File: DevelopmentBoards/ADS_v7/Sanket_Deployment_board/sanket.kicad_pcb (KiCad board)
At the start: 2 copper layers, 95.9 x 92 mm, 42 parts, among them J2 Conn_02x03_Counter_Clockwise, J3 Conn_02x03_Counter_Clockwise, U1 SN74LVC1G17QDCKRQ1

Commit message: ADS-V7, Corrected board setting according to PCB power, placed resistors after the decoupling capacitors
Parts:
- moved R12 12.2 mm to (129.2, 133.6), turned to -90 degrees
- moved R10 6.95 mm to (129.2, 137.5), turned to 90 degrees
- moved J1 3.26 mm to (132.9, 130.4)
- moved L1 1.28 mm to (130.8, 143.2)
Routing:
- net +3V3: track 97.5 -> 92.6 mm
- net Net-(J1-Pin_1): track 6.71 -> 9.95 mm
- net /BurnWire1IN: track 84.9 -> 81.7 mm
- net Net-(J1-Pin_3): track 7.44 -> 4.90 mm
- net Net-(D1-K): track 30.9 -> 32.1 mm

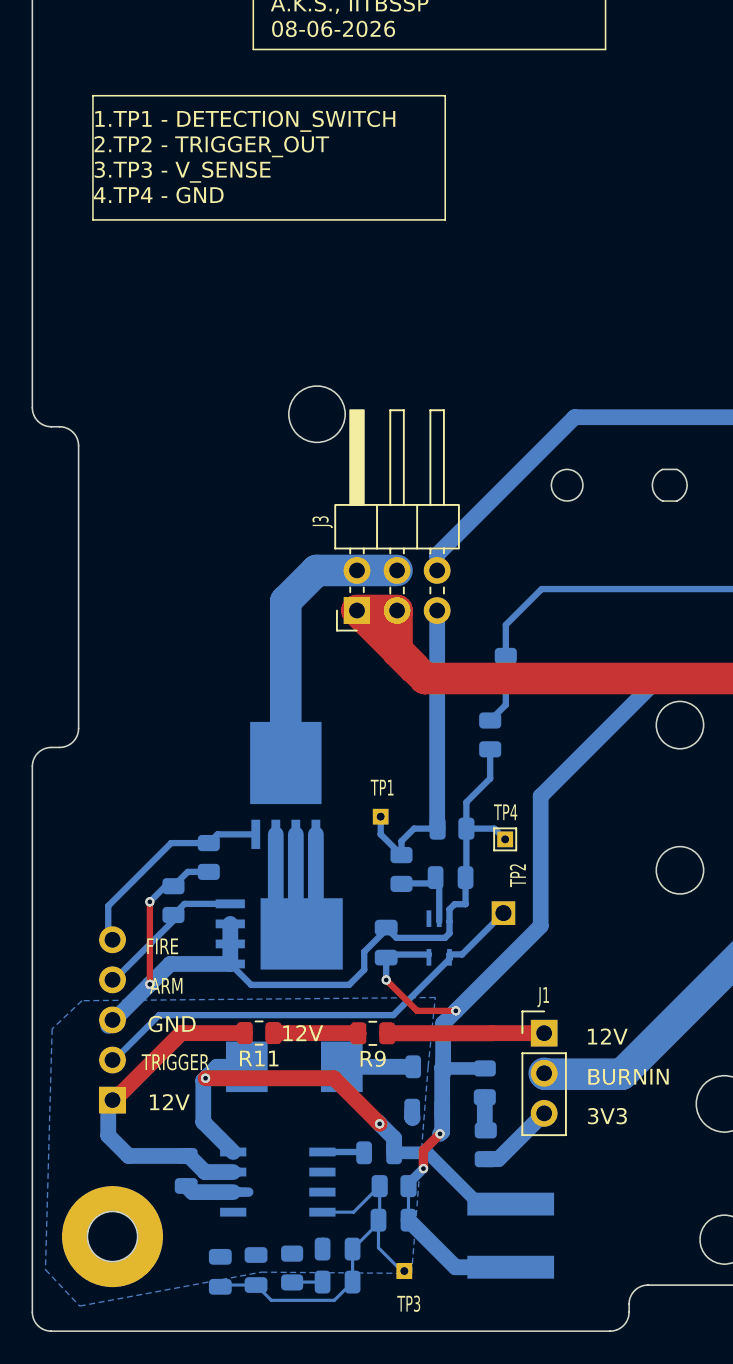
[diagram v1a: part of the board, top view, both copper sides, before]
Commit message: ADSV7- Corrected routing of TPS5420 convertor according to its datasheet
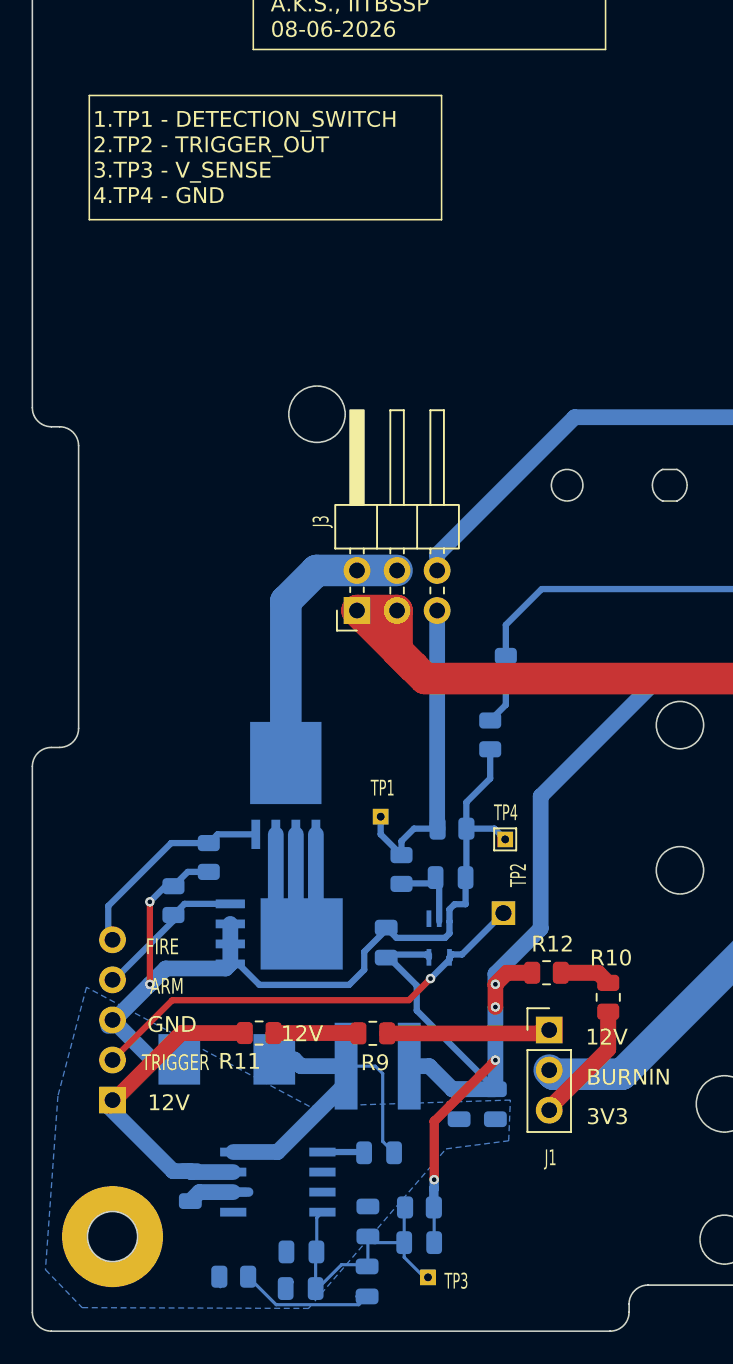
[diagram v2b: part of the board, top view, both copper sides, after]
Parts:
- R10, R12: moved to F.Cu
- moved L1 13.7 mm to (122.4, 132.5), turned to 0 degrees
- moved R10 12.1 mm to (137.0, 128.1)
- moved R12 8.00 mm to (133.1, 126.6), turned to 0 degrees
- moved C7 5.20 mm to (117.5, 146.6), turned to 0 degrees
- moved C4 4.34 mm to (129.8, 134.9), turned to 90 degrees
- moved D1 4.31 mm to (112.8, 132.1), turned to 180 degrees
- moved R6 3.74 mm to (113.3, 145.8), turned to 180 degrees
- moved C6 3.10 mm to (117.5, 144.3), turned to 0 degrees
- moved C5 3.08 mm to (127.5, 134.9), turned to 90 degrees
- moved R7 2.60 mm to (121.8, 142.3), turned to 90 degrees
- moved C9 2.16 mm to (125.0, 143.7)
- moved R8 2.10 mm to (125.0, 141.5)
- moved C8 1.87 mm to (121.7, 146.1), turned to 90 degrees
- moved TP3 1.55 mm to (125.6, 145.9)
- moved C10 0.99 mm to (110.5, 140.1)
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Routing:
- net Net-(D1-K): track 32.1 -> 22.6 mm, vias 2 -> 0
- net +3V3: track 92.6 -> 100.5 mm
- net Net-(C8-Pad1): track 1.94 -> 9.15 mm
- net Net-(U3-VSNS): track 24.8 -> 19.5 mm
- net Net-(J1-Pin_3): track 4.90 -> 7.79 mm
- net +12V: track 22.3 -> 20.2 mm
- net GND: track 65.4 -> 64.0 mm
- net Net-(R10-Pad2): track 2.12 -> 3.26 mm
- net /TriggerOUT: track 29.7 -> 29.2 mm, vias 0 -> 1

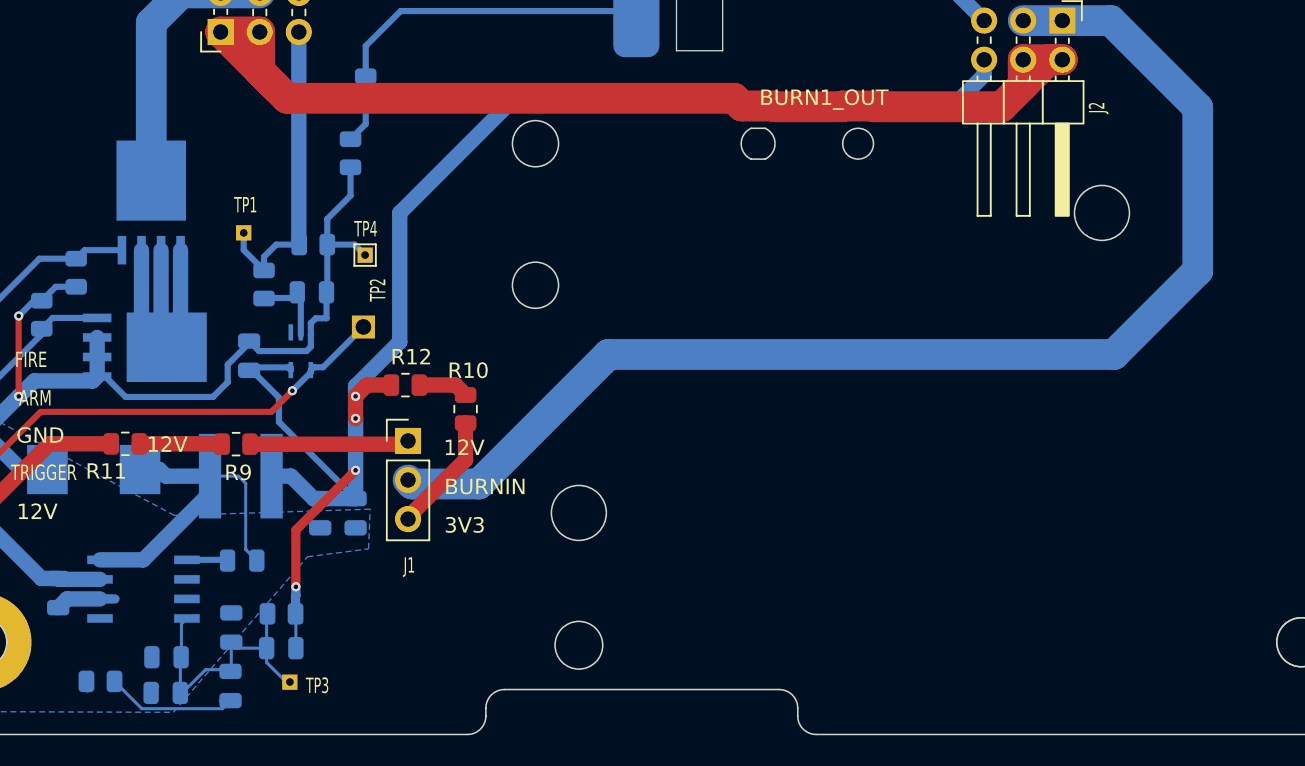
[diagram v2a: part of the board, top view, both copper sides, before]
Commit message: ADS v7: Corrected layout of converter, replaced tp pads with thp pads in resistor board, some other minor trace layout changes
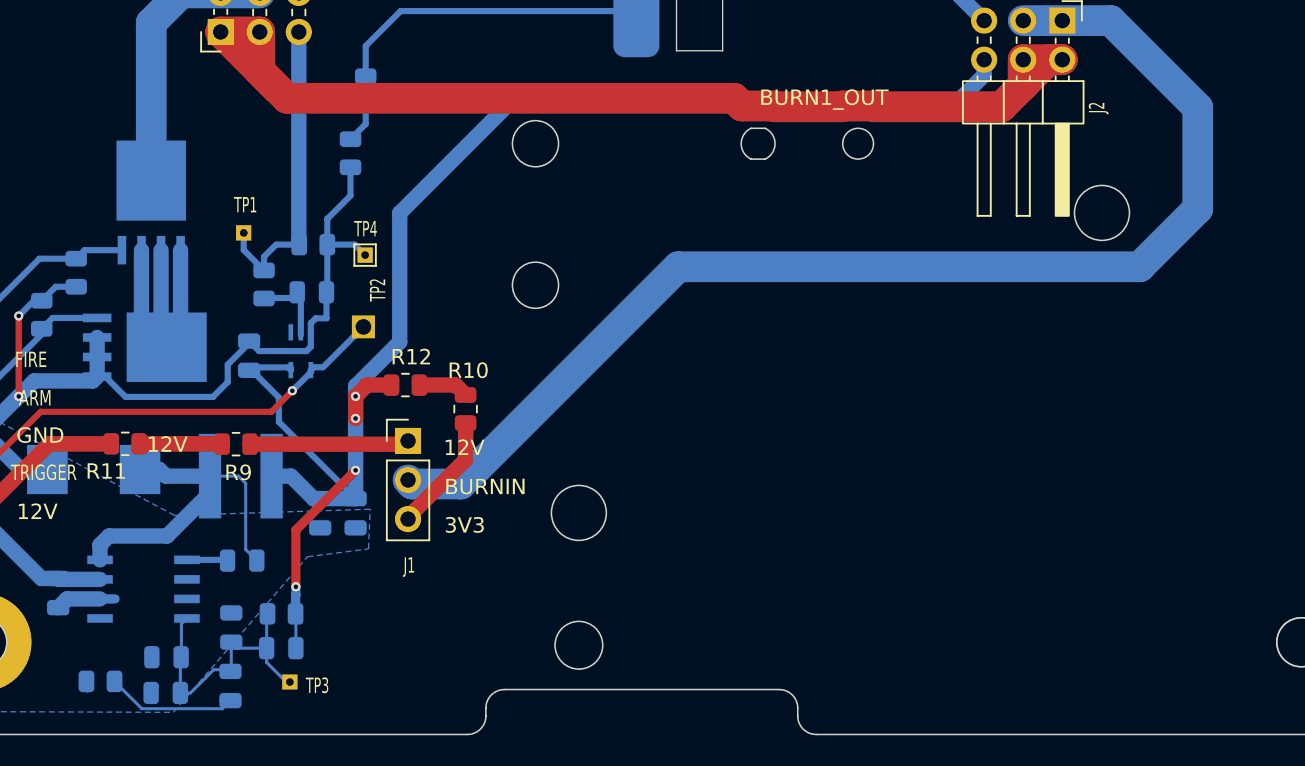
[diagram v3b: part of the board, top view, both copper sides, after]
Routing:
- net /BurnWire1IN: track 81.5 -> 79.1 mm
- net Net-(D1-K): track 22.6 -> 23.2 mm
